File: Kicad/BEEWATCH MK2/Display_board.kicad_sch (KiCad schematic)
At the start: 4 parts, among them J4 Conn_02x06_Odd_Even

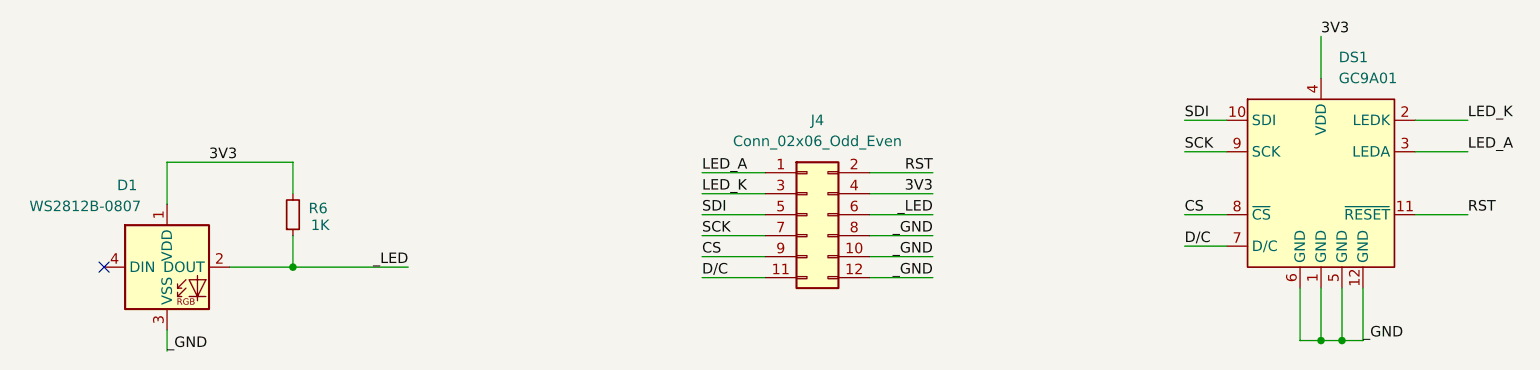
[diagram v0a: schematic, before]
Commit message: Added Display board schema
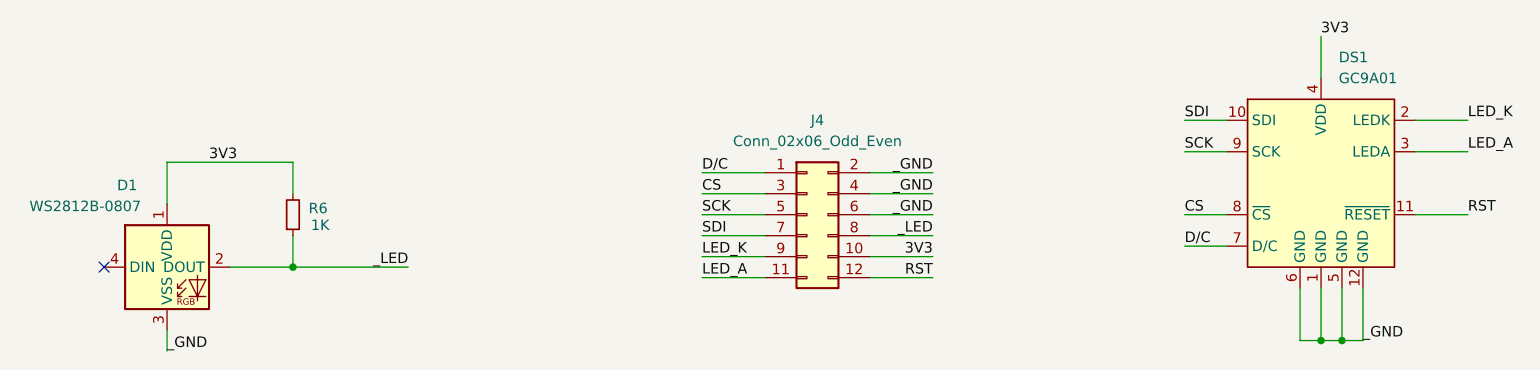
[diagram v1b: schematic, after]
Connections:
- net 3V3: now also J4.10 (Pin_10); no longer J4.4 (Pin_4)
- net CS: now also J4.3 (Pin_3); no longer J4.9 (Pin_9)
- net D/C: now also J4.1 (Pin_1); no longer J4.11 (Pin_11)
- net LED_A: now also J4.11 (Pin_11); no longer J4.1 (Pin_1)
- net LED_K: now also J4.9 (Pin_9); no longer J4.3 (Pin_3)
- net RST: now also J4.12 (Pin_12); no longer J4.2 (Pin_2)
- net SCK: now also J4.5 (Pin_5); no longer J4.7 (Pin_7)
- net SDI: now also J4.7 (Pin_7); no longer J4.5 (Pin_5)
- net _GND: now also J4.2 (Pin_2), J4.4 (Pin_4), J4.6 (Pin_6); no longer J4.10 (Pin_10), J4.12 (Pin_12), J4.8 (Pin_8)
- net _LED: now also J4.8 (Pin_8); no longer J4.6 (Pin_6)
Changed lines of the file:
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@@
 	)
 	(label "_GND"
-		(at 177.8 87.63 180)
-		(effects
-			(font
-				(size 1.27 1.27)
-			)
-			(justify right bottom)
-		)
-	)
-	(label "_GND"
-		(at 177.8 85.09 180)
+		(at 177.8 80.01 180)
+		(effects
+			(font
+				(size 1.27 1.27)
+			)
+			(justify right bottom)
+		)
+	)
+	(label "_GND"
+		(at 177.8 82.55 180)
 		(effects
 			(font
@@
 	)
 	(label "RST"
-		(at 177.8 77.47 180)
+		(at 177.8 90.17 180)
 		(effects
 			(font
@@
 	)
 	(label "_LED"
-		(at 177.8 82.55 180)
+		(at 177.8 85.09 180)
 		(effects
 			(font
@@
 	)
 	(label "SDI"
-		(at 149.86 82.55 0)
+		(at 149.86 85.09 0)
 		(effects
 			(font
@@
 	)
 	(label "LED_K"
-		(at 149.86 80.01 0)
+		(at 149.86 87.63 0)
 		(effects
 			(font
@@
 	)
 	(label "SCK"
-		(at 149.86 85.09 0)
+		(at 149.86 82.55 0)
 		(effects
 			(font
@@
 	)
 	(label "LED_A"
-		(at 149.86 77.47 0)
+		(at 149.86 90.17 0)
 		(effects
 			(font
@@
 	)
 	(label "D{slash}C"
-		(at 149.86 90.17 0)
+		(at 149.86 77.47 0)
 		(effects
 			(font
@@
 	)
 	(label "CS"
-		(at 149.86 87.63 0)
+		(at 149.86 80.01 0)
 		(effects
 			(font
@@
 	)
 	(label "3V3"
-		(at 177.8 80.01 180)
-		(effects
-			(font
-				(size 1.27 1.27)
-			)
-			(justify right bottom)
-		)
-	)
-	(label "_GND"
-		(at 177.8 90.17 180)
-		(effects
-			(font
+		(at 177.8 87.63 180)
+		(effects
+			(font
+				(size 1.27 1.27)
+			)
+			(justify right bottom)
+		)
+	)
+	(label "_GND"
+		(at 177.8 77.47 180)
+		(effects
+			(font

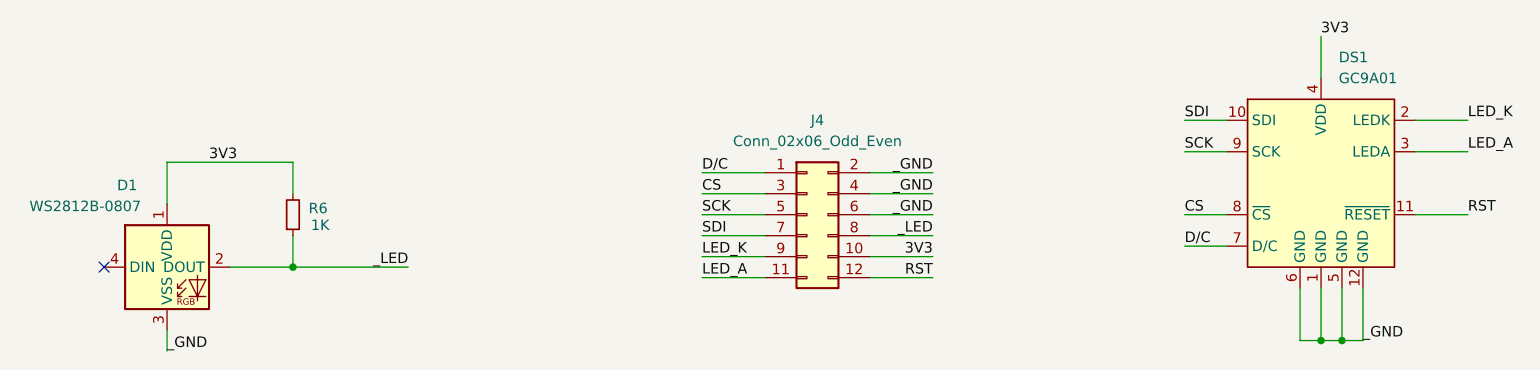
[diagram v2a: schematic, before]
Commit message: Updating MPN
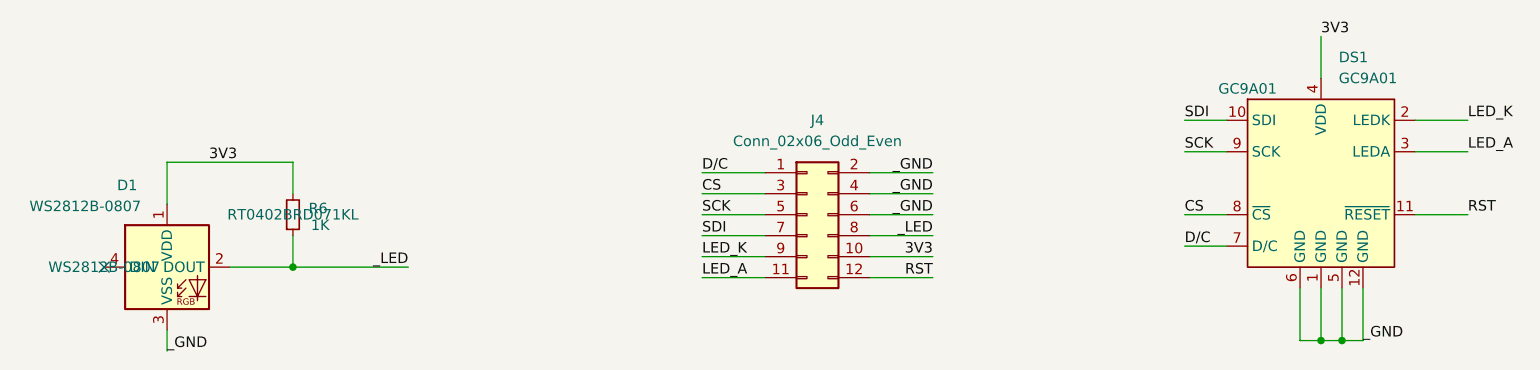
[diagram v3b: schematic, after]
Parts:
- D1: MPN (none) -> WS2812B-0807
- DS1: MPN (none) -> GC9A01
- R6: MPN (none) -> RT0402BRD071KL
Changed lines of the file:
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@@
 			)
 		)
-		(property "MPN" ""
+		(property "MPN" "RT0402BRD071KL "
 			(at 100.33 82.55 0)
 			(effects
@@
 			)
 		)
-		(property "MPN" ""
+		(property "MPN" "WS2812B-0807"
 			(at 77.47 88.9 0)
 			(effects
@@
 			)
 		)
-		(property "MPN" ""
-			(at 215.9 67.31 0)
-			(effects
+		(property "MPN" "GC9A01"
+			(at 215.9 67.31 0)
+			(effects
